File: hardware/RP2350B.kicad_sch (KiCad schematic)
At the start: 41 parts, among them SW1 SMD_Pushbutton, SW2 SMD_Pushbutton, U1 RP2350B-QFN80, U2 W25Q32JVSS, Y1 ABM8-272-T3

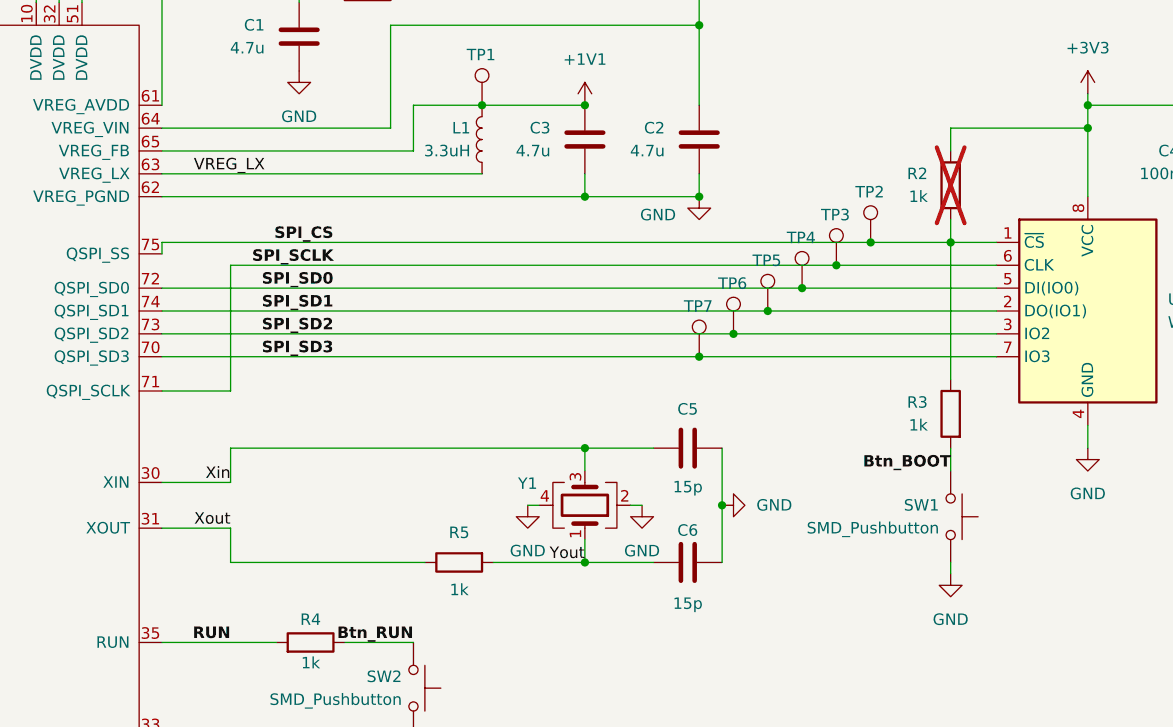
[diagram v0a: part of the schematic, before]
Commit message: fixed short to GND on CLKOUT0
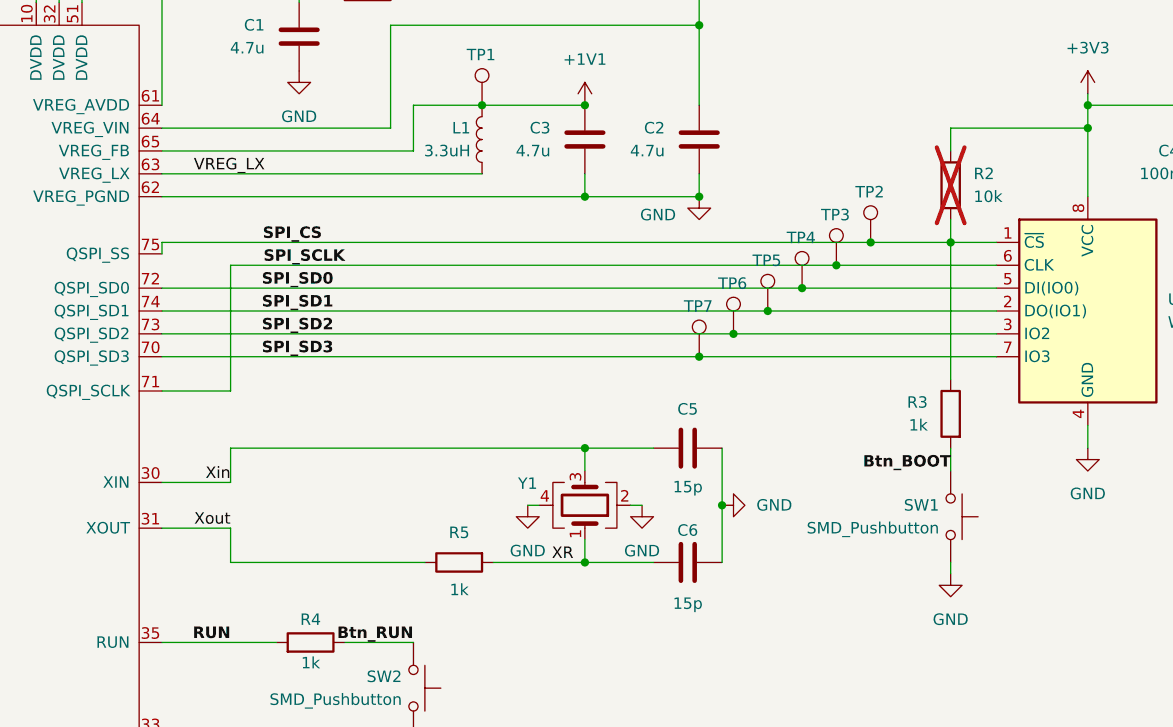
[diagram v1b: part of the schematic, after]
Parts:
- R2: value 1k -> 10k
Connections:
- net Yout renamed XR
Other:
- company: (none) -> Nico Zehetner
- title: (none) -> PIcroscope - A RP2350 based Microscope
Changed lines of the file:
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@@
 	(generator_version "8.0")
 	(paper "A4")
+	(title_block
+		(title "PIcroscope - A RP2350 based Microscope")
+		(date "2025-05-13")
+		(rev "V0.2")
+		(company "Nico Zehetner")
+	)
 	(junction
 		(at 172.72 73.66)
@@
 	(wire
 		(pts
-			(xy 191.77 60.96) (xy 113.03 60.96)
-		)
-		(stroke
-			(width 0)
-			(type default)
-		)
-	)
-	(wire
-		(pts
 			(xy 175.26 83.82) (xy 175.26 90.17)
 		)
@@
 	(wire
 		(pts
-			(xy 187.96 63.5) (xy 120.65 63.5)
+			(xy 113.03 60.96) (xy 191.77 60.96)
 		)
 		(stroke
@@
 	(wire
 		(pts
+			(xy 120.65 63.5) (xy 187.96 63.5)
+		)
+		(stroke
+			(width 0)
+			(type default)
+		)
+	)
+	(wire
+		(pts
 			(xy 91.44 29.21) (xy 91.44 34.29)
 		)
@@
 	(wire
 		(pts
-			(xy 160.02 96.52) (xy 149.86 96.52)
+			(xy 149.86 96.52) (xy 160.02 96.52)
 		)
 		(stroke
@@
 		)
 	)
-	(label "Yout"
-		(at 160.02 96.52 180)
+	(label "XR"
+		(at 158.75 96.52 180)
 		(fields_autoplaced yes)
 		(effects
@@
 	)
 	(label "SPI_SCLK"
-		(at 132.08 63.5 180)
+		(at 133.35 63.5 180)
 		(fields_autoplaced yes)
 		(effects
@@
 	)
 	(label "SPI_CS"
-		(at 132.08 60.96 180)
+		(at 130.81 60.96 180)
 		(fields_autoplaced yes)
 		(effects
@@
 		(fields_autoplaced yes)
 		(property "Reference" "R2"
-			(at 198.12 53.3399 0)
+			(at 203.2 53.3399 0)
 			(effects
 				(font
 					(size 1.27 1.27)
 				)
-				(justify left)
+				(justify right)
 			)
 		)
-		(property "Value" "1k"
-			(at 198.12 55.8799 0)
+		(property "Value" "10k"
+			(at 203.2 55.8799 0)
 			(effects
 				(font
 					(size 1.27 1.27)
 				)
-				(justify left)
+				(justify right)
 			)
 		)
